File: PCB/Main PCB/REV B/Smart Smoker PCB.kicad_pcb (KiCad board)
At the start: 4 copper layers, 120 x 60 mm, 90 parts, among them J1 1051330001, J10 Ignitor, J11 Auger, J12 FAN, J2 393570002, J3 393570002, J4 393570002, J5 393570002, J6 393570002, J7 Hopper, J8 Lid, J9 MEM2051-00-195-00-A, K1 CPC1966Y, Q1 25V 1.5A Trans, Q2 25V 1.5A Trans, Q3 Q_PMOS_GSD, Q4 Q_PMOS_GSD, SW1 SW_Coded_SH-7050, U1 ESP32-WROOM-32UE_16MB, U2 DG409LEDY-T1-GE3, U3 MAX31855KASA, U4 CP2102N-Axx-xQFN20, U5 AMS1117-3.3, U6 LTC4412xS6, U7 AQH3223A, U8 AQH3223A

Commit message: Begin layout Rev B PCB
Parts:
- removed Q3, Q4: Q_PMOS_GSD, Package_TO_SOT_SMD:SOT-23
- removed SW1: SW_Coded_SH-7050, Rotary_Encoder:PAC18R1-43D19F
- added C19: 0.1uF 50V X7R 0603, Capacitor_SMD:C_0603_1608Metric, F.Cu at (74.8, 143.0)
- added C20: 0.1uF 50V X7R 0603, Capacitor_SMD:C_0603_1608Metric, F.Cu at (70.8, 143.0)
- added C21: Film 0.1uF 305V 15mm, Capacitor_THT:C_Rect_L18.0mm_W6.0mm_P15.00mm_FKS3_FKP3, F.Cu at (127.5, 79.4)
- added C22: Film 0.1uF 305V 15mm, Capacitor_THT:C_Rect_L18.0mm_W6.0mm_P15.00mm_FKS3_FKP3, F.Cu at (150.6, 74.4)
- added MT1: PEC11R-4215F-S0024, Customs Smoker:XDCR_PEC11R-4215F-S0024, F.Cu at (28.0, 78.0)
- added R23: 10K 1% 0603, Resistor_SMD:R_0603_1608Metric, F.Cu at (69.0, 146.0)
- added R24: 250Ohm 0.1% 0603, Resistor_SMD:R_0603_1608Metric, F.Cu at (65.0, 149.0)
- added R25: 105Ohm 1% 0603, Resistor_SMD:R_0603_1608Metric, F.Cu at (146.7, 93.9)
- added R26: 105Ohm 1% 0603, Resistor_SMD:R_0603_1608Metric, F.Cu at (139.3, 87.0)
- added R27: 47Ohm 5% 1/2W, Resistor_THT:R_Axial_DIN0204_L3.6mm_D1.6mm_P5.08mm_Vertical, F.Cu at (138.8, 91.1)
- added R28: 105Ohm 1% 0603, Resistor_SMD:R_0603_1608Metric, F.Cu at (139.3, 84.5)
- added R29: 47Ohm 5% 1/2W, Resistor_THT:R_Axial_DIN0204_L3.6mm_D1.6mm_P5.08mm_Vertical, F.Cu at (147.0, 91.1)
- C10: value 0.1uF 50V X7R 0603 -> 0.01uF 50V X7R 0603
- C11: value 10uF 16V X5R 0805 -> 0.01uF 50V X7R 0603; footprint Capacitor_SMD:C_0805_2012Metric -> Capacitor_SMD:C_0603_1608Metric
- C12, C13: value 10uF 16V X5R 0805 -> 0.1uF 50V X7R 0603; footprint Capacitor_SMD:C_0805_2012Metric -> Capacitor_SMD:C_0603_1608Metric
- C15: value 1uF 25V X5R 0603 -> 10uF 16V X5R 0805; footprint Capacitor_SMD:C_0603_1608Metric -> Capacitor_SMD:C_0805_2012Metric
- C16: value 0.1uF 50V X7R 0603 -> 10uF 16V X5R 0805; footprint Capacitor_SMD:C_0603_1608Metric -> Capacitor_SMD:C_0805_2012Metric
- C17: value Film 0.1uF 305V 15mm -> 10uF 16V X5R 0805; footprint Capacitor_THT:C_Rect_L18.0mm_W6.0mm_P15.00mm_FKS3_FKP3 -> Capacitor_SMD:C_0805_2012Metric
- C18: value Film 0.1uF 305V 15mm -> 1uF 16V X7R 0603; footprint Capacitor_THT:C_Rect_L18.0mm_W6.0mm_P15.00mm_FKS3_FKP3 -> Capacitor_SMD:C_0603_1608Metric
- C6: value 4.7uF 25V X5R 0805 -> 0.1uF 50V X7R 0603; footprint Capacitor_SMD:C_0805_2012Metric -> Capacitor_SMD:C_0603_1608Metric
- C8: value 0.1uF 50V X7R 0603 -> 4.7uF 25V X5R 0805; footprint Capacitor_SMD:C_0603_1608Metric -> Capacitor_SMD:C_0805_2012Metric
- J1: value 1051330001 -> 393570002; footprint Customs Smoker:1051330001_MOL -> Customs Smoker:CONN_393570002_MOL
- J2, J4: value 393570002 -> MJ-3502; footprint Customs Smoker:CONN_393570002_MOL -> Customs Smoker:CUI_MJ-3502
- J3: value 393570002 -> 1051330001; footprint Customs Smoker:CONN_393570002_MOL -> Customs Smoker:1051330001_MOL
- J5, J6: value 393570002 -> MJ-3502; footprint Customs Smoker:CONN_393570002_MOL -> TestPoint:TestPoint_2Pads_Pitch5.08mm_Drill1.3mm
- J8: value Lid -> Micro_SD_Card_Det; footprint Connector_Molex:Molex_Micro-Fit_3.0_43045-0400_2x02_P3.00mm_Horizontal -> Customs Smoker:DM3CS-SF_HIR
- J9: value MEM2051-00-195-00-A -> Lid; footprint Customs Smoker:GCT_MEM2051-00-195-00-A -> Connector_Molex:Molex_Micro-Fit_3.0_43045-0400_2x02_P3.00mm_Horizontal
- PS1: moved to B.Cu
- R16: value 0Ohm 0603 -> 10K 1% 0603
- R17: value 470Ohm 5% 0603 -> 0Ohm 0603
- R18, R19, R21: value 105Ohm 1% 0603 -> 10K 1% 0603
- R20, R22: value 47Ohm 5% 1/2W -> 10K 1% 0603; footprint Resistor_THT:R_Axial_DIN0204_L3.6mm_D1.6mm_P5.08mm_Vertical -> Resistor_SMD:R_0603_1608Metric
- R3: value 470Ohm 1% 0603 -> 10K 1% 0603
- R4: value 10K 1% 0603 -> 470Ohm 1% 0603
- S3: moved to F.Cu
- U6: value LTC4412xS6 -> TPS2115APWR; footprint Package_TO_SOT_SMD:TSOT-23-6 -> Customs Smoker:SOP65P640X120-8N
- moved R18 159.5 mm to (25.0, 96.0)
- moved U1 152.3 mm to (51.5, 38.0)
- moved J1 152.2 mm to (67.1, 100.4)
- moved R20 150.1 mm to (23.8, 91.2)
- moved C13 149.6 mm to (254.0, 57.0)
- moved C14 146.0 mm to (254.0, 54.2)
- moved C17 133.2 mm to (37.3, 164.2)
- moved J4 132.1 mm to (253.0, 34.0), turned to 0 degrees
- moved R21 130.9 mm to (24.0, 94.0)
- moved R19 125.8 mm to (29.0, 93.5)
- moved C4 121.4 mm to (224.0, 47.0)
- moved J8 120.4 mm to (108.0, 34.0)
- moved J5 119.4 mm to (241.5, 26.0), turned to 0 degrees
- moved C15 115.3 mm to (32.9, 164.2)
- moved D5 115.0 mm to (138.0, 39.0), turned to 0 degrees
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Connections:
- C10 pad 1: GND -> /IO32
- C10 pad 2: +3.3VA -> GND
- C11 pad 1: +3.3VA -> /IO33
- C12 pad 1: +5V -> +3.3V
- C13 pad 1: +3.3VP -> GND
- C13 pad 2: GND -> +3.3VA
- C14 pad 1: +3.3VP -> +3.3VA
- C15 pad 1: GND -> +5V
- C15 pad 2: +3.3V -> GND
- C16 pad 1: +3.3VA -> +3.3VP
- C17 pad 1: /Loads/Auger_- -> +3.3VP
- C17 pad 2: Net-(C17-Pad2) -> GND
- C18 pad 1: /Loads/Auger_- -> GND
- C18 pad 2: Net-(C18-Pad2) -> +3.3V
- C5 pad 1: GND -> /EN
- C5 pad 2: +3.3V -> GND
- C6 pad 1: GND -> /IO0
- C6 pad 2: +3.3V -> GND
- C7 pad 1: /EN -> GND
- C7 pad 2: GND -> +3.3V
- C8 pad 1: /IO0 -> GND
- C8 pad 2: GND -> +3.3V
- J1 pad 1: +5V -> /AC_L
- J1 pad 2: /USB_DN -> /AC_N
- J2 pad 1: /Probe4+ -> /Probe1-
- J2 pad 2: /Probe4- -> /Probe1+
- J3 pad 1: /AC_L -> +5V
- J3 pad 2: /AC_N -> /USB_DN
- J4 pad 1: /Probe1+ -> /Probe2-
- J4 pad 2: /Probe1- -> /Probe2+
- J5 pad 1: /Probe2+ -> /Probe3-
- J5 pad 2: /Probe2- -> /Probe3+
- J6 pad 1: /Probe3+ -> /Probe4-
- J6 pad 2: /Probe3- -> /Probe4+
- J8 pad 1: /I2C_SDA -> unconnected-(J8-Pad1)
- J8 pad 2: GND -> /IO15
- J8 pad 3: /I2C_SCL -> /SPI_MOSI
- J9 pad 1: unconnected-(J9-Pad1) -> /I2C_SDA
- J9 pad 2: unconnected-(J9-Pad2) -> GND
- J9 pad 3: unconnected-(J9-Pad3) -> /I2C_SCL
- J9 pad 4: unconnected-(J9-Pad4) -> +3.3V
- R16 pad 1: /RXD0 -> /IO34
- R16 pad 2: /TXD -> +3.3V
- R17 pad 1: /Power/IO4 -> /RXD0
- R17 pad 2: +3.3V -> /TXD
- R18 pad 1: /Loads/IGNITOR -> Net-(MT1-PadA)
- R18 pad 2: Net-(K1-Pad2) -> /IO33
- R19 pad 1: /Loads/AUGER -> Net-(MT1-PadB)
- R19 pad 2: Net-(R19-Pad2) -> /IO32
- R20 pad 1: Net-(C17-Pad2) -> +3.3V
- R20 pad 2: /Loads/AC_N -> Net-(MT1-PadB)
- R21 pad 1: /Loads/FAN -> +3.3V
- R21 pad 2: Net-(R21-Pad2) -> Net-(MT1-PadA)
- R22 pad 1: Net-(C18-Pad2) -> +3.3V
- R22 pad 2: /Loads/AC_N -> Net-(J8-Pad9)
- R3 pad 1: +3.3V -> /EN
- R3 pad 2: Net-(D1-Pad2) -> +3.3V
- R4 pad 1: /EN -> +3.3V
- R4 pad 2: +3.3V -> Net-(D1-Pad2)
- U1 pad 27: /IO16 -> /SPI_MOSI
- U2 pad 16: /IO15 -> /IO16
- U6 pad 1: +3.3VA -> /Power/IO_4
- U6 pad 2: GND -> unconnected-(U6-Pad2)
- U6 pad 4: /Power/IO4 -> Net-(R24-Pad1)
- U6 pad 5: Net-(Q4-Pad1) -> GND
- U6 pad 6: +3.3V -> +3.3VA
- U7 pad 2: Net-(R19-Pad2) -> Net-(R26-Pad2)
- U8 pad 2: Net-(R21-Pad2) -> Net-(R28-Pad2)

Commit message: PCB schematic updates, Find mosfet for relay on circuit
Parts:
- removed the C12 at (109.0, 44.0)
- removed the C21 at (127.5, 79.4)
- removed the J8 at (108.0, 34.0)
- removed K1: CPC1966Y, Customs Smoker:SIP4_CPC1966Y_LTF
- removed the R23 at (69.0, 146.0)
- removed the R27 at (138.8, 91.1)
- removed the R28 at (139.3, 84.5)
- removed S3: RR511D1121, Customs Smoker:E-SWITCH_RR511D1121
- added C15: 0.1uF 50V X7R 0603, Capacitor_SMD:C_0603_1608Metric, F.Cu at (164.0, 130.0)
- added C16: 10uF 16V X5R 0805, Capacitor_SMD:C_0805_2012Metric, F.Cu at (159.8, 130.2)
- added C22: 0.1uF 50V X7R 0603, Capacitor_SMD:C_0603_1608Metric, F.Cu at (230.0, 115.0)
- added C23: 0.1uF 50V X7R 0603, Capacitor_SMD:C_0603_1608Metric, F.Cu at (226.0, 115.0)
- added C24: 0.1uF 50V X7R 0603, Capacitor_SMD:C_0603_1608Metric, F.Cu at (222.0, 115.0)
- added PS2: IRM-05-5, Converter_ACDC:Converter_ACDC_MeanWell_IRM-05-xx_THT, F.Cu at (162.1, 113.8)
- added R24: 140Ohm 1% 0603, Resistor_SMD:R_0603_1608Metric, F.Cu at (230.0, 112.5)
- added R26: 140Ohm 1% 0603, Resistor_SMD:R_0603_1608Metric, F.Cu at (222.0, 112.5)
- added U10: ALDP105W, Customs Smoker:PAN_ALD_PAN, F.Cu at (236.8, 94.9)
- added U11: ALDP105W, Customs Smoker:PAN_ALD_PAN, F.Cu at (248.5, 94.9)
- added U12: TLP2362TPR_E, Customs Smoker:TLP2362, F.Cu at (260.0, 101.9)
- added U9: TLP2362TPR_E, Customs Smoker:TLP2362, F.Cu at (260.0, 107.7)
- R22: value 10K 1% 0603 -> 50Ohm 0.1% 0603
- R25: value 105Ohm 1% 0603 -> 140Ohm 1% 0603
- U5: renamed from U6; footprint Customs Smoker:SOP65P640X120-8N -> Customs Smoker:PW8-M
- U7: value AQH3223A -> ALDP105W; footprint Package_SO:SSO-7-8_6.4x9.78mm_P2.54mm -> Customs Smoker:PAN_ALD_PAN
- U8: value AQH3223A -> TLP2362TPR_E; footprint Package_SO:SSO-7-8_6.4x9.78mm_P2.54mm -> Customs Smoker:TLP2362
- moved U8 129.0 mm to (260.0, 96.0)
- moved R22 113.4 mm to (207.0, 103.0)
- moved R25 81.4 mm to (226.0, 112.5)
- moved U7 56.6 mm to (162.6, 139.3)
- renumbered C13 to C12, C14 to C13, C18 to C14, C19 to C17, C20 to C18, C15 to C19, C16 to C20, C17 to C21, C22 to C25, J11 to J10, J10 to J11, J9 to J8, J12 to J9, R24 to R23, R26 to R27, R29 to R28, U5 to U6
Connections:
- C1 pad 1: GND -> +5V
- C10 pad 2: GND -> +5V
- C11 pad 2: GND -> +5V
- C12 pad 1: GND -> +5V
- C13 pad 2: GND -> +5V
- C14 pad 1: GND -> +5V
- C17 pad 1: GND -> +5V
- C18 pad 1: GND -> +5V
- C19 pad 1: +5V -> +5VA
- C19 pad 2: GND -> +5V
- C2 pad 1: GND -> +5V
- C20 pad 2: GND -> +5V
- C21 pad 2: GND -> +5V
- C25 pad 1: /Loads/Auger_- -> /Loads/Fan_-
- C3 pad 2: GND -> +5V
- C5 pad 2: GND -> +5V
- C6 pad 2: GND -> +5V
- C7 pad 1: GND -> +5V
- C8 pad 1: GND -> +5V
- C9 pad 1: +5V -> +5VA
- C9 pad 2: GND -> +5V
- D2 pad 1: GND -> +5V
- D3 pad 1: GND -> +5V
- D5 pad 1: GND -> +5V
- D5 pad 4: +5V -> +5VA
- H1 pad 1: GND -> +5V
- J11 pad 2: /Loads/Auger_- -> /Loads/Heater_-
- J3 pad 1: +5V -> +5VA
- J3 pad 5: GND -> +5V
- J7 pad 2: GND -> +5V
- J8 pad 2: GND -> +5V
- J9 pad 2: /Loads/Auger_- -> /Loads/Fan_-
- MT1 pad 1: GND -> +5V
- MT1 pad COM: GND -> +5V
- MT1 pad S1: GND -> +5V
- MT1 pad S2: GND -> +5V
- PS1 pad 3: GND -> +5V
- R15 pad 1: GND -> +5V
- R22 pad 1: +3.3V -> +5V
- R22 pad 2: Net-(J8-Pad9) -> +3.3V
- R23 pad 2: GND -> +5V
- R25 pad 1: /Loads/IGNITOR -> /Loads/FAN
- R27 pad 2: Net-(R26-Pad2) -> unconnected-(R27-Pad2)
- S1 pad 1: GND -> +5V
- S2 pad 1: GND -> +5V
- TP2 pad 1: GND -> +5V
- TP3 pad 1: GND -> +5V
- TP9 pad 3: GND -> +5V
- U1 pad 1: GND -> +5V
- U1 pad 15: GND -> +5V
- U1 pad 38: GND -> +5V
- U1 pad 39: GND -> +5V
- U1 pad 40: GND -> +5V
- U1 pad 41: GND -> +5V
- U1 pad 42: GND -> +5V
- U1 pad 43: GND -> +5V
- U1 pad 44: GND -> +5V
- U1 pad 45: GND -> +5V
- U1 pad 46: GND -> +5V
- U1 pad 47: GND -> +5V
- U2 pad 15: GND -> +5V
- U2 pad 3: GND -> +5V
- U3 pad 1: GND -> +5V
- U4 pad 2: GND -> +5V
- U4 pad 25: GND -> +5V
- U5 pad 1: /Power/IO_4 -> unconnected-(U5-Pad1)
- U5 pad 3: GND -> +5V
- U5 pad 5: GND -> +5V
- U6 pad 1: GND -> +5V
- U6 pad 3: +5V -> +5VA
- U7 pad 1: GND -> unconnected-(U7-Pad1)
- U7 pad 2: Net-(R26-Pad2) -> unconnected-(U7-Pad2)
- U7 pad 3: GND -> unconnected-(U7-Pad3)
- U7 pad 4: GND -> unconnected-(U7-Pad4)
- U8 pad 1: GND -> Net-(R24-Pad2)
- U8 pad 3: GND -> +5V
- U8 pad 4: GND -> Net-(C22-Pad2)
- U8 pad 5: unconnected-(U8-Pad5) -> /Loads/Opto_Auger
- U8 pad 6: /Loads/AC_N -> +5V

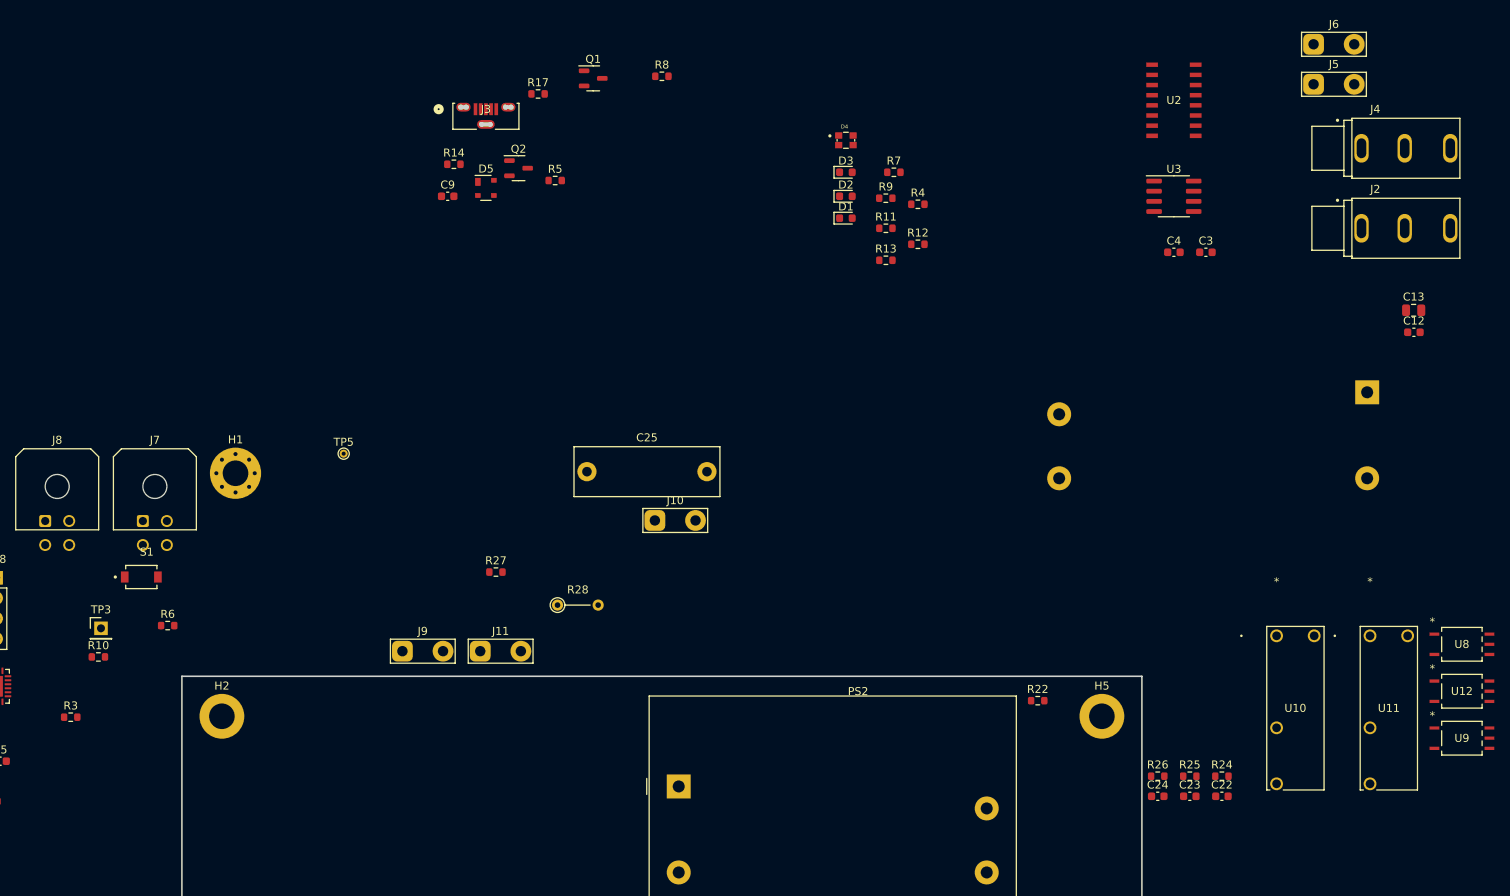
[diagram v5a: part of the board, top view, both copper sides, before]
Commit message: PCB schematic updates, Thermocouple connector sourced and updated
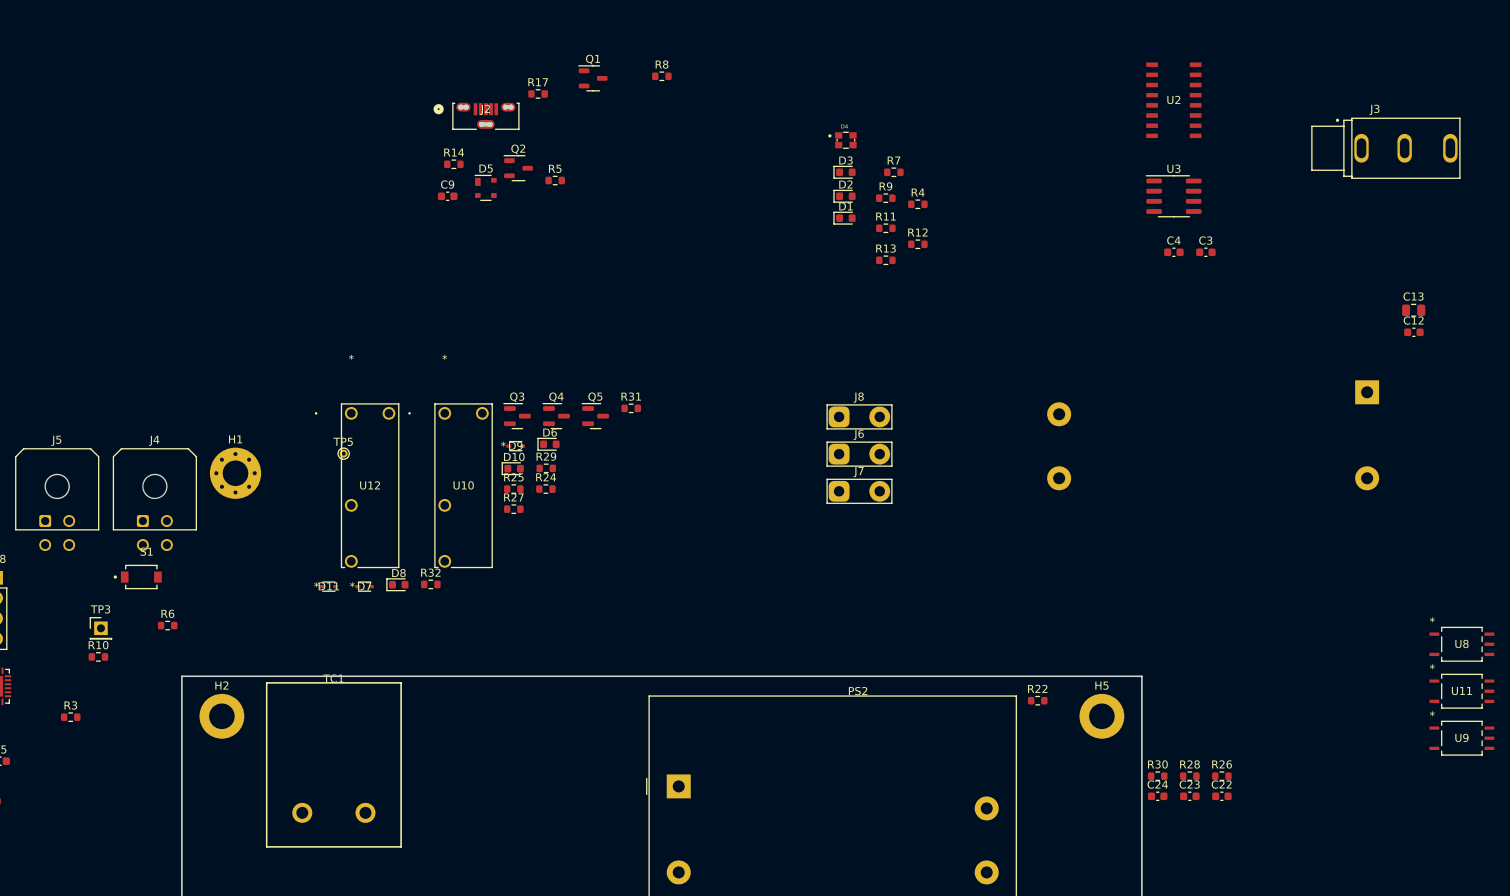
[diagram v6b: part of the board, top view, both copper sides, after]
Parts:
- removed C25: Film 0.1uF 305V 15mm, Capacitor_THT:C_Rect_L18.0mm_W6.0mm_P15.00mm_FKS3_FKP3
- removed J10: Auger, TestPoint:TestPoint_2Pads_Pitch5.08mm_Drill1.3mm
- removed J11: Ignitor, TestPoint:TestPoint_2Pads_Pitch5.08mm_Drill1.3mm
- removed the J2 at (253.0, 44.0)
- removed the J5 at (241.5, 26.0)
- removed J9: FAN, TestPoint:TestPoint_2Pads_Pitch5.08mm_Drill1.3mm
- removed the R28 at (147.0, 91.1)
- removed the U11 at (248.5, 94.9)
- added D10: B 3.2 20mA 0603, LED_SMD:LED_0603_1608Metric, F.Cu at (141.5, 74.0)
- added D11: Schottky 30v 200mA, Customs Smoker:RB521S30T1G-M, F.Cu at (118.4, 88.8)
- added D6: B 3.2 20mA 0603, LED_SMD:LED_0603_1608Metric, F.Cu at (146.0, 71.0)
- added D7: Schottky 30v 200mA, Customs Smoker:RB521S30T1G-M, F.Cu at (122.8, 88.8)
- added D8: B 3.2 20mA 0603, LED_SMD:LED_0603_1608Metric, F.Cu at (127.1, 88.6)
- added D9: Schottky 30v 200mA, Customs Smoker:RB521S30T1G-M, F.Cu at (141.7, 71.2)
- added J7: Auger, TestPoint:TestPoint_2Pads_Pitch5.08mm_Drill1.3mm, F.Cu at (182.2, 76.9)
- added J8: Fan, TestPoint:TestPoint_2Pads_Pitch5.08mm_Drill1.3mm, F.Cu at (182.2, 67.6)
- added Q3: 2N7002, Package_TO_SOT_SMD:SOT-23, F.Cu at (141.9, 67.5)
- added Q4: 2N7002, Package_TO_SOT_SMD:SOT-23, F.Cu at (146.8, 67.5)
- added Q5: 2N7002, Package_TO_SOT_SMD:SOT-23, F.Cu at (151.7, 67.5)
- added R24: 91Ohm 1% 0603, Resistor_SMD:R_0603_1608Metric, F.Cu at (145.5, 76.6)
- added R25: 0 Ohm 0603, Resistor_SMD:R_0603_1608Metric, F.Cu at (141.5, 76.6)
- added R29: 0 Ohm 0603, Resistor_SMD:R_0603_1608Metric, F.Cu at (145.5, 74.0)
- added R31: 91Ohm 1% 0603, Resistor_SMD:R_0603_1608Metric, F.Cu at (156.2, 66.5)
- added R32: 0 Ohm 0603, Resistor_SMD:R_0603_1608Metric, F.Cu at (131.1, 88.5)
- added TC1: Thermocouple_Block, Customs Smoker:K-TypeAdapter, F.Cu at (119.0, 100.8)
- added U12: ALDP105W, Customs Smoker:PAN_ALD_PAN, F.Cu at (121.2, 67.1)
- J6: value MJ-3502 -> Ignitor
- R27: value 105Ohm 1% 0603 -> 91Ohm 1% 0603
- moved U10 107.6 mm to (132.9, 67.1)
- moved J6 78.4 mm to (182.2, 72.2)
- moved R27 8.17 mm to (141.5, 79.1)
- renumbered J3 to J2, J4 to J3, J7 to J4, J8 to J5, R24 to R26, R25 to R28, R26 to R30, U12 to U11
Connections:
- J6 pad 1: /Probe4- -> /Ignitor_+
- J6 pad 2: /Probe4+ -> /Ignitor_-
- R27 pad 1: /Loads/AUGER -> +5V
- R27 pad 2: unconnected-(R27-Pad2) -> Net-(D8-Pad2)
- U10 pad 1: unconnected-(U10-Pad1) -> +5V
- U10 pad 2: unconnected-(U10-Pad2) -> /Loads/AC_L
- U10 pad 3: unconnected-(U10-Pad3) -> /Loads/Ignitor_+
- U10 pad 4: unconnected-(U10-Pad4) -> Net-(D9-Pad2)
- U7 pad 1: unconnected-(U7-Pad1) -> +5V
- U7 pad 2: unconnected-(U7-Pad2) -> /Loads/AC_L
- U7 pad 3: unconnected-(U7-Pad3) -> /Loads/Auger_+
- U7 pad 4: unconnected-(U7-Pad4) -> Net-(U7-Pad4)
